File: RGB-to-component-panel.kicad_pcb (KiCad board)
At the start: 2 copper layers, 50 x 70 mm, 60 parts, among them J1 VGA, J3 USB_C_Receptacle_Power, J4 SCART_CONN, J5 3xRCA_CONN, U1 SC6206B-65K5, U101 TPF144-VR, U2 TPF144-VR, U3 RS8752XQ, U6 74AHC1G86, U7 74AHC1G86, U8 LM1881

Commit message: fixed resistor
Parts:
- removed the C1 at (37.8, 77.5)
- removed the C10 at (38.9, 52.7)
- removed the C11 at (57.1, 68.0)
- removed the C12 at (44.9, 90.7)
- removed the C13 at (39.5, 63.3)
- removed the C14 at (45.0, 68.7)
- removed the C2 at (37.8, 81.3)
- removed the C3 at (37.8, 88.9)
- removed the C4 at (40.3, 75.9)
- removed the C5 at (33.7, 44.5)
- removed the C7 at (51.0, 48.0)
- removed the C8 at (39.5, 44.1)
- removed the C9 at (44.6, 49.6)
- removed the D101 at (58.0, 46.9)
- removed the GOTE1 at (54.0, 96.6)
- removed the GOTE2 at (47.8, 80.7)
- removed the J1 at (24.6, 75.0)
- removed the J3 at (18.4, 47.6)
- removed the J4 at (29.4, 98.0)
- removed the J5 at (66.0, 62.0)
- removed the JP1 at (45.5, 57.0)
- removed the JR1 at (69.7, 90.6)
- removed the JU1 at (69.7, 103.6)
- removed the L101 at (30.6, 43.1)
- removed the R1 at (44.6, 47.6)
- removed the R10 at (56.9, 79.0)
- removed the R101 at (54.8, 49.6)
- removed the R11 at (59.0, 69.6)
- removed the R12 at (52.6, 60.0)
- removed the R13 at (50.6, 60.0)
- removed the R14 at (57.1, 64.2)
- removed the R15 at (39.5, 59.4)
- removed the R16 at (29.6, 46.2)
- removed the R17 at (29.6, 48.2)
- removed the R18 at (45.0, 70.7)
- removed the R19 at (33.8, 52.7)
- removed the R2 at (40.8, 47.6)
- removed the R20 at (45.6, 80.7)
- removed the R21 at (45.6, 82.7)
- removed the R22 at (45.6, 84.7)
- removed the R23 at (42.5, 83.6)
- removed the R24 at (57.1, 71.9)
- removed the R25 at (55.1, 71.9)
- removed the R26 at (52.8, 71.9)
- removed the R27 at (48.8, 71.9)
- removed the R28 at (50.8, 71.9)
- removed the R3 at (37.8, 73.7)
- removed the R4 at (37.8, 85.1)
- removed the R5 at (37.8, 92.7)
- removed the R6 at (56.6, 60.0)
- removed the R7 at (54.6, 60.0)
- removed the R8 at (54.9, 79.0)
- removed the R9 at (57.9, 54.0)
- removed the U1 at (42.7, 44.1)
- removed the U101 at (43.6, 76.6)
- removed the U2 at (44.9, 88.0)
- removed the U3 at (54.1, 66.0)
- removed the U6 at (33.8, 55.6)
- removed the U7 at (38.8, 55.6)
- removed the U8 at (45.0, 64.9)
- added C1: 1u, Capacitor_SMD:C_0805_2012Metric_Pad1.15x1.40mm_HandSolder, F.Cu at (37.6, 77.5)
- added C1: 1u, Capacitor_SMD:C_0805_2012Metric_Pad1.15x1.40mm_HandSolder, F.Cu at (90.6, 77.5)
- added C1: 1u, Capacitor_SMD:C_0805_2012Metric_Pad1.15x1.40mm_HandSolder, F.Cu at (37.6, 150.5)
- added C1: 1u, Capacitor_SMD:C_0805_2012Metric_Pad1.15x1.40mm_HandSolder, F.Cu at (90.6, 150.5)
- added C10: 100n, Capacitor_SMD:C_0805_2012Metric_Pad1.15x1.40mm_HandSolder, F.Cu at (38.7, 52.7)
- added C10: 100n, Capacitor_SMD:C_0805_2012Metric_Pad1.15x1.40mm_HandSolder, F.Cu at (91.7, 52.7)
- added C10: 100n, Capacitor_SMD:C_0805_2012Metric_Pad1.15x1.40mm_HandSolder, F.Cu at (38.7, 125.7)
- added C10: 100n, Capacitor_SMD:C_0805_2012Metric_Pad1.15x1.40mm_HandSolder, F.Cu at (91.7, 125.7)
- added C11: 100n, Capacitor_SMD:C_0805_2012Metric_Pad1.15x1.40mm_HandSolder, F.Cu at (56.9, 68.0)
- added C11: 100n, Capacitor_SMD:C_0805_2012Metric_Pad1.15x1.40mm_HandSolder, F.Cu at (109.9, 68.0)
- added C11: 100n, Capacitor_SMD:C_0805_2012Metric_Pad1.15x1.40mm_HandSolder, F.Cu at (56.9, 141.0)
- added C11: 100n, Capacitor_SMD:C_0805_2012Metric_Pad1.15x1.40mm_HandSolder, F.Cu at (109.9, 141.0)
- added C12: 100n, Capacitor_SMD:C_0805_2012Metric_Pad1.15x1.40mm_HandSolder, F.Cu at (44.7, 90.7)
- added C12: 100n, Capacitor_SMD:C_0805_2012Metric_Pad1.15x1.40mm_HandSolder, F.Cu at (97.7, 90.7)
- added C12: 100n, Capacitor_SMD:C_0805_2012Metric_Pad1.15x1.40mm_HandSolder, F.Cu at (44.7, 163.7)
- added C12: 100n, Capacitor_SMD:C_0805_2012Metric_Pad1.15x1.40mm_HandSolder, F.Cu at (97.7, 163.7)
- added C13: 100n, Capacitor_SMD:C_0805_2012Metric_Pad1.15x1.40mm_HandSolder, F.Cu at (39.3, 63.3)
- added C13: 100n, Capacitor_SMD:C_0805_2012Metric_Pad1.15x1.40mm_HandSolder, F.Cu at (92.3, 63.3)
- added C13: 100n, Capacitor_SMD:C_0805_2012Metric_Pad1.15x1.40mm_HandSolder, F.Cu at (39.3, 136.3)
- added C13: 100n, Capacitor_SMD:C_0805_2012Metric_Pad1.15x1.40mm_HandSolder, F.Cu at (92.3, 136.3)
- added C14: 100n, Capacitor_SMD:C_0805_2012Metric_Pad1.15x1.40mm_HandSolder, F.Cu at (44.8, 68.7)
- added C14: 100n, Capacitor_SMD:C_0805_2012Metric_Pad1.15x1.40mm_HandSolder, F.Cu at (97.8, 68.7)
- added C14: 100n, Capacitor_SMD:C_0805_2012Metric_Pad1.15x1.40mm_HandSolder, F.Cu at (44.8, 141.7)
- added C14: 100n, Capacitor_SMD:C_0805_2012Metric_Pad1.15x1.40mm_HandSolder, F.Cu at (97.8, 141.7)
- added C2: 1u, Capacitor_SMD:C_0805_2012Metric_Pad1.15x1.40mm_HandSolder, F.Cu at (37.6, 81.3)
- added C2: 1u, Capacitor_SMD:C_0805_2012Metric_Pad1.15x1.40mm_HandSolder, F.Cu at (90.6, 81.3)
- added C2: 1u, Capacitor_SMD:C_0805_2012Metric_Pad1.15x1.40mm_HandSolder, F.Cu at (37.6, 154.3)
- added C2: 1u, Capacitor_SMD:C_0805_2012Metric_Pad1.15x1.40mm_HandSolder, F.Cu at (90.6, 154.3)
- added C3: 1u, Capacitor_SMD:C_0805_2012Metric_Pad1.15x1.40mm_HandSolder, F.Cu at (37.6, 88.9)
- added C3: 1u, Capacitor_SMD:C_0805_2012Metric_Pad1.15x1.40mm_HandSolder, F.Cu at (90.6, 88.9)
- added C3: 1u, Capacitor_SMD:C_0805_2012Metric_Pad1.15x1.40mm_HandSolder, F.Cu at (37.6, 161.9)
- added C3: 1u, Capacitor_SMD:C_0805_2012Metric_Pad1.15x1.40mm_HandSolder, F.Cu at (90.6, 161.9)
- added C4: 100n, Capacitor_SMD:C_0805_2012Metric_Pad1.15x1.40mm_HandSolder, F.Cu at (40.1, 75.9)
- added C4: 100n, Capacitor_SMD:C_0805_2012Metric_Pad1.15x1.40mm_HandSolder, F.Cu at (93.1, 75.9)
- added C4: 100n, Capacitor_SMD:C_0805_2012Metric_Pad1.15x1.40mm_HandSolder, F.Cu at (40.1, 148.9)
- added C4: 100n, Capacitor_SMD:C_0805_2012Metric_Pad1.15x1.40mm_HandSolder, F.Cu at (93.1, 148.9)
- added C5: 10u, Capacitor_Tantalum_SMD:CP_EIA-3216-18_Kemet-A_Pad1.58x1.35mm_HandSolder, F.Cu at (33.5, 44.5)
- added C5: 10u, Capacitor_Tantalum_SMD:CP_EIA-3216-18_Kemet-A_Pad1.58x1.35mm_HandSolder, F.Cu at (86.5, 44.5)
- added C5: 10u, Capacitor_Tantalum_SMD:CP_EIA-3216-18_Kemet-A_Pad1.58x1.35mm_HandSolder, F.Cu at (33.5, 117.5)
- added C5: 10u, Capacitor_Tantalum_SMD:CP_EIA-3216-18_Kemet-A_Pad1.58x1.35mm_HandSolder, F.Cu at (86.5, 117.5)
- added C7: 100u, Capacitor_Tantalum_SMD:CP_EIA-3528-21_Kemet-B_Pad1.50x2.35mm_HandSolder, F.Cu at (50.8, 48.0)
- added C7: 100u, Capacitor_Tantalum_SMD:CP_EIA-3528-21_Kemet-B_Pad1.50x2.35mm_HandSolder, F.Cu at (103.8, 48.0)
- added C7: 100u, Capacitor_Tantalum_SMD:CP_EIA-3528-21_Kemet-B_Pad1.50x2.35mm_HandSolder, F.Cu at (50.8, 121.0)
- added C7: 100u, Capacitor_Tantalum_SMD:CP_EIA-3528-21_Kemet-B_Pad1.50x2.35mm_HandSolder, F.Cu at (103.8, 121.0)
- added C8: 100n, Capacitor_SMD:C_0805_2012Metric_Pad1.15x1.40mm_HandSolder, F.Cu at (39.3, 44.1)
- added C8: 100n, Capacitor_SMD:C_0805_2012Metric_Pad1.15x1.40mm_HandSolder, F.Cu at (92.3, 44.1)
- added C8: 100n, Capacitor_SMD:C_0805_2012Metric_Pad1.15x1.40mm_HandSolder, F.Cu at (39.3, 117.1)
- added C8: 100n, Capacitor_SMD:C_0805_2012Metric_Pad1.15x1.40mm_HandSolder, F.Cu at (92.3, 117.1)
- added C9: 10u, Capacitor_SMD:C_0805_2012Metric_Pad1.15x1.40mm_HandSolder, F.Cu at (44.4, 49.6)
- added C9: 10u, Capacitor_SMD:C_0805_2012Metric_Pad1.15x1.40mm_HandSolder, F.Cu at (97.4, 49.6)
- added C9: 10u, Capacitor_SMD:C_0805_2012Metric_Pad1.15x1.40mm_HandSolder, F.Cu at (44.4, 122.6)
- added C9: 10u, Capacitor_SMD:C_0805_2012Metric_Pad1.15x1.40mm_HandSolder, F.Cu at (97.4, 122.6)
- added D101: LED, LED_SMD:LED_0805_2012Metric, F.Cu at (57.8, 46.9)
- added D101: LED, LED_SMD:LED_0805_2012Metric, F.Cu at (110.8, 46.9)
- added D101: LED, LED_SMD:LED_0805_2012Metric, F.Cu at (57.8, 119.9)
- added D101: LED, LED_SMD:LED_0805_2012Metric, F.Cu at (110.8, 119.9)
- added GOTE1: Fiducial, videobits:uwuriel, F.Cu at (53.8, 96.6)
- added GOTE1: Fiducial, videobits:uwuriel, F.Cu at (106.8, 96.6)
- added GOTE1: Fiducial, videobits:uwuriel, F.Cu at (53.8, 169.6)
- added GOTE1: Fiducial, videobits:uwuriel, F.Cu at (106.8, 169.6)
- added GOTE2: Fiducial, videobits:borgar, B.Cu at (47.6, 80.7)
- added GOTE2: Fiducial, videobits:borgar, B.Cu at (100.6, 80.7)
- added GOTE2: Fiducial, videobits:borgar, B.Cu at (47.6, 153.7)
- added GOTE2: Fiducial, videobits:borgar, B.Cu at (100.6, 153.7)
- added J1: VGA, custom_components:VGA_CONN, F.Cu at (24.4, 75.0)
- added J1: VGA, custom_components:VGA_CONN, F.Cu at (77.4, 75.0)
- added J1: VGA, custom_components:VGA_CONN, F.Cu at (24.4, 148.0)
- added J1: VGA, custom_components:VGA_CONN, F.Cu at (77.4, 148.0)
- added J3: USB_C_Receptacle_Power, videobits:USB_C_Receptacle_Generic_Power_Only, F.Cu at (18.2, 47.6)
- added J3: USB_C_Receptacle_Power, videobits:USB_C_Receptacle_Generic_Power_Only, F.Cu at (71.2, 47.6)
- added J3: USB_C_Receptacle_Power, videobits:USB_C_Receptacle_Generic_Power_Only, F.Cu at (18.2, 120.6)
- added J3: USB_C_Receptacle_Power, videobits:USB_C_Receptacle_Generic_Power_Only, F.Cu at (71.2, 120.6)
- added J4: SCART_CONN, custom_components:SCART_CONN, F.Cu at (29.2, 98.0)
- added J4: SCART_CONN, custom_components:SCART_CONN, F.Cu at (82.2, 98.0)
- added J4: SCART_CONN, custom_components:SCART_CONN, F.Cu at (29.2, 171.0)
- added J4: SCART_CONN, custom_components:SCART_CONN, F.Cu at (82.2, 171.0)
- added J5: 3xRCA_CONN, custom_components:3xRCA_CONN, F.Cu at (65.8, 62.0)
- added J5: 3xRCA_CONN, custom_components:3xRCA_CONN, F.Cu at (118.8, 62.0)
- added J5: 3xRCA_CONN, custom_components:3xRCA_CONN, F.Cu at (65.8, 135.0)
- added J5: 3xRCA_CONN, custom_components:3xRCA_CONN, F.Cu at (118.8, 135.0)
- added JP1: Jumper_3_Bridged12, Jumper:SolderJumper-3_P1.3mm_Bridged12_Pad1.0x1.5mm, F.Cu at (45.3, 57.0)
- added JP1: Jumper_3_Bridged12, Jumper:SolderJumper-3_P1.3mm_Bridged12_Pad1.0x1.5mm, F.Cu at (98.3, 57.0)
- added JP1: Jumper_3_Bridged12, Jumper:SolderJumper-3_P1.3mm_Bridged12_Pad1.0x1.5mm, F.Cu at (45.3, 130.0)
- added JP1: Jumper_3_Bridged12, Jumper:SolderJumper-3_P1.3mm_Bridged12_Pad1.0x1.5mm, F.Cu at (98.3, 130.0)
- added JR1: Conn_Coaxial, videobits:Cheapo_RCA_single_edge, F.Cu at (69.5, 90.6)
- added JR1: Conn_Coaxial, videobits:Cheapo_RCA_single_edge, F.Cu at (122.5, 90.6)
- added JR1: Conn_Coaxial, videobits:Cheapo_RCA_single_edge, F.Cu at (69.5, 163.6)
- added JR1: Conn_Coaxial, videobits:Cheapo_RCA_single_edge, F.Cu at (122.5, 163.6)
- added JU1: Conn_Coaxial, videobits:Cheapo_RCA_single_edge, F.Cu at (69.5, 103.6)
- added JU1: Conn_Coaxial, videobits:Cheapo_RCA_single_edge, F.Cu at (122.5, 103.6)
- added JU1: Conn_Coaxial, videobits:Cheapo_RCA_single_edge, F.Cu at (69.5, 176.6)
- added JU1: Conn_Coaxial, videobits:Cheapo_RCA_single_edge, F.Cu at (122.5, 176.6)
- added L101: 10u, Inductor_SMD:L_0805_2012Metric_Pad1.15x1.40mm_HandSolder, F.Cu at (30.4, 43.1)
- added L101: 10u, Inductor_SMD:L_0805_2012Metric_Pad1.15x1.40mm_HandSolder, F.Cu at (83.4, 43.1)
- added L101: 10u, Inductor_SMD:L_0805_2012Metric_Pad1.15x1.40mm_HandSolder, F.Cu at (30.4, 116.1)
- added L101: 10u, Inductor_SMD:L_0805_2012Metric_Pad1.15x1.40mm_HandSolder, F.Cu at (83.4, 116.1)
- added R1: 1k, Resistor_SMD:R_0805_2012Metric_Pad1.15x1.40mm_HandSolder, F.Cu at (44.4, 47.6)
- added R1: 1k, Resistor_SMD:R_0805_2012Metric_Pad1.15x1.40mm_HandSolder, F.Cu at (97.4, 47.6)
- added R1: 1k, Resistor_SMD:R_0805_2012Metric_Pad1.15x1.40mm_HandSolder, F.Cu at (44.4, 120.6)
- added R1: 1k, Resistor_SMD:R_0805_2012Metric_Pad1.15x1.40mm_HandSolder, F.Cu at (97.4, 120.6)
- added R10: 75, Resistor_SMD:R_0805_2012Metric_Pad1.15x1.40mm_HandSolder, F.Cu at (56.7, 79.0)
- added R10: 75, Resistor_SMD:R_0805_2012Metric_Pad1.15x1.40mm_HandSolder, F.Cu at (109.7, 79.0)
- added R10: 75, Resistor_SMD:R_0805_2012Metric_Pad1.15x1.40mm_HandSolder, F.Cu at (56.7, 152.0)
- added R10: 75, Resistor_SMD:R_0805_2012Metric_Pad1.15x1.40mm_HandSolder, F.Cu at (109.7, 152.0)
- added R101: 1k, Resistor_SMD:R_0805_2012Metric_Pad1.15x1.40mm_HandSolder, F.Cu at (54.6, 49.6)
- added R101: 1k, Resistor_SMD:R_0805_2012Metric_Pad1.15x1.40mm_HandSolder, F.Cu at (107.6, 49.6)
- added R101: 1k, Resistor_SMD:R_0805_2012Metric_Pad1.15x1.40mm_HandSolder, F.Cu at (54.6, 122.6)
- added R101: 1k, Resistor_SMD:R_0805_2012Metric_Pad1.15x1.40mm_HandSolder, F.Cu at (107.6, 122.6)
- added R11: 75, Resistor_SMD:R_0805_2012Metric_Pad1.15x1.40mm_HandSolder, F.Cu at (58.8, 69.6)
- added R11: 75, Resistor_SMD:R_0805_2012Metric_Pad1.15x1.40mm_HandSolder, F.Cu at (111.8, 69.6)
- added R11: 75, Resistor_SMD:R_0805_2012Metric_Pad1.15x1.40mm_HandSolder, F.Cu at (58.8, 142.6)
- added R11: 75, Resistor_SMD:R_0805_2012Metric_Pad1.15x1.40mm_HandSolder, F.Cu at (111.8, 142.6)
- added R12: 4k7, Resistor_SMD:R_0805_2012Metric_Pad1.15x1.40mm_HandSolder, F.Cu at (52.4, 60.0)
- added R12: 4k7, Resistor_SMD:R_0805_2012Metric_Pad1.15x1.40mm_HandSolder, F.Cu at (105.4, 60.0)
- added R12: 4k7, Resistor_SMD:R_0805_2012Metric_Pad1.15x1.40mm_HandSolder, F.Cu at (52.4, 133.0)
- added R12: 4k7, Resistor_SMD:R_0805_2012Metric_Pad1.15x1.40mm_HandSolder, F.Cu at (105.4, 133.0)
- added R13: 1k27, Resistor_SMD:R_0805_2012Metric_Pad1.15x1.40mm_HandSolder, F.Cu at (50.4, 60.0)
- added R13: 1k27, Resistor_SMD:R_0805_2012Metric_Pad1.15x1.40mm_HandSolder, F.Cu at (103.4, 60.0)
- added R13: 1k27, Resistor_SMD:R_0805_2012Metric_Pad1.15x1.40mm_HandSolder, F.Cu at (50.4, 133.0)
- added R13: 1k27, Resistor_SMD:R_0805_2012Metric_Pad1.15x1.40mm_HandSolder, F.Cu at (103.4, 133.0)
- added R14: 1k, Resistor_SMD:R_0805_2012Metric_Pad1.15x1.40mm_HandSolder, F.Cu at (56.9, 64.2)
- added R14: 1k, Resistor_SMD:R_0805_2012Metric_Pad1.15x1.40mm_HandSolder, F.Cu at (109.9, 64.2)
- added R14: 1k, Resistor_SMD:R_0805_2012Metric_Pad1.15x1.40mm_HandSolder, F.Cu at (56.9, 137.2)
- added R14: 1k, Resistor_SMD:R_0805_2012Metric_Pad1.15x1.40mm_HandSolder, F.Cu at (109.9, 137.2)
- added R15: 75, Resistor_SMD:R_0805_2012Metric_Pad1.15x1.40mm_HandSolder, F.Cu at (39.3, 59.4)
- added R15: 75, Resistor_SMD:R_0805_2012Metric_Pad1.15x1.40mm_HandSolder, F.Cu at (92.3, 59.4)
- added R15: 75, Resistor_SMD:R_0805_2012Metric_Pad1.15x1.40mm_HandSolder, F.Cu at (39.3, 132.4)
- added R15: 75, Resistor_SMD:R_0805_2012Metric_Pad1.15x1.40mm_HandSolder, F.Cu at (92.3, 132.4)
- added R16: 5k1, Resistor_SMD:R_0805_2012Metric_Pad1.15x1.40mm_HandSolder, F.Cu at (29.4, 46.2)
- added R16: 5k1, Resistor_SMD:R_0805_2012Metric_Pad1.15x1.40mm_HandSolder, F.Cu at (82.4, 46.2)
- added R16: 5k1, Resistor_SMD:R_0805_2012Metric_Pad1.15x1.40mm_HandSolder, F.Cu at (29.4, 119.2)
- added R16: 5k1, Resistor_SMD:R_0805_2012Metric_Pad1.15x1.40mm_HandSolder, F.Cu at (82.4, 119.2)
- added R17: 5k1, Resistor_SMD:R_0805_2012Metric_Pad1.15x1.40mm_HandSolder, F.Cu at (29.4, 48.2)
- added R17: 5k1, Resistor_SMD:R_0805_2012Metric_Pad1.15x1.40mm_HandSolder, F.Cu at (82.4, 48.2)
- added R17: 5k1, Resistor_SMD:R_0805_2012Metric_Pad1.15x1.40mm_HandSolder, F.Cu at (29.4, 121.2)
- added R17: 5k1, Resistor_SMD:R_0805_2012Metric_Pad1.15x1.40mm_HandSolder, F.Cu at (82.4, 121.2)
- added R18: 680k, Resistor_SMD:R_0805_2012Metric_Pad1.15x1.40mm_HandSolder, F.Cu at (44.8, 70.7)
- added R18: 680k, Resistor_SMD:R_0805_2012Metric_Pad1.15x1.40mm_HandSolder, F.Cu at (97.8, 70.7)
- added R18: 680k, Resistor_SMD:R_0805_2012Metric_Pad1.15x1.40mm_HandSolder, F.Cu at (44.8, 143.7)
- added R18: 680k, Resistor_SMD:R_0805_2012Metric_Pad1.15x1.40mm_HandSolder, F.Cu at (97.8, 143.7)
- added R19: 1k, Resistor_SMD:R_0805_2012Metric_Pad1.15x1.40mm_HandSolder, F.Cu at (33.6, 52.7)
- added R19: 1k, Resistor_SMD:R_0805_2012Metric_Pad1.15x1.40mm_HandSolder, F.Cu at (86.6, 52.7)
- added R19: 1k, Resistor_SMD:R_0805_2012Metric_Pad1.15x1.40mm_HandSolder, F.Cu at (33.6, 125.7)
- added R19: 1k, Resistor_SMD:R_0805_2012Metric_Pad1.15x1.40mm_HandSolder, F.Cu at (86.6, 125.7)
- added R2: 1k33, Resistor_SMD:R_0805_2012Metric_Pad1.15x1.40mm_HandSolder, F.Cu at (40.6, 47.6)
- added R2: 1k33, Resistor_SMD:R_0805_2012Metric_Pad1.15x1.40mm_HandSolder, F.Cu at (93.6, 47.6)
- added R2: 1k33, Resistor_SMD:R_0805_2012Metric_Pad1.15x1.40mm_HandSolder, F.Cu at (40.6, 120.6)
- added R2: 1k33, Resistor_SMD:R_0805_2012Metric_Pad1.15x1.40mm_HandSolder, F.Cu at (93.6, 120.6)
- added R20: 1k, Resistor_SMD:R_0805_2012Metric_Pad1.15x1.40mm_HandSolder, F.Cu at (45.4, 80.7)
- added R20: 1k, Resistor_SMD:R_0805_2012Metric_Pad1.15x1.40mm_HandSolder, F.Cu at (98.4, 80.7)
- added R20: 1k, Resistor_SMD:R_0805_2012Metric_Pad1.15x1.40mm_HandSolder, F.Cu at (45.4, 153.7)
- added R20: 1k, Resistor_SMD:R_0805_2012Metric_Pad1.15x1.40mm_HandSolder, F.Cu at (98.4, 153.7)
- added R21: 511, Resistor_SMD:R_0805_2012Metric_Pad1.15x1.40mm_HandSolder, F.Cu at (45.4, 82.7)
- added R21: 511, Resistor_SMD:R_0805_2012Metric_Pad1.15x1.40mm_HandSolder, F.Cu at (98.4, 82.7)
- added R21: 511, Resistor_SMD:R_0805_2012Metric_Pad1.15x1.40mm_HandSolder, F.Cu at (45.4, 155.7)
- added R21: 511, Resistor_SMD:R_0805_2012Metric_Pad1.15x1.40mm_HandSolder, F.Cu at (98.4, 155.7)
- added R22: 2740, Resistor_SMD:R_0805_2012Metric_Pad1.15x1.40mm_HandSolder, F.Cu at (45.4, 84.7)
- added R22: 2740, Resistor_SMD:R_0805_2012Metric_Pad1.15x1.40mm_HandSolder, F.Cu at (98.4, 84.7)
- added R22: 2740, Resistor_SMD:R_0805_2012Metric_Pad1.15x1.40mm_HandSolder, F.Cu at (45.4, 157.7)
- added R22: 2740, Resistor_SMD:R_0805_2012Metric_Pad1.15x1.40mm_HandSolder, F.Cu at (98.4, 157.7)
- added R23: 300, Resistor_SMD:R_0805_2012Metric_Pad1.15x1.40mm_HandSolder, F.Cu at (42.3, 83.6)
- added R23: 300, Resistor_SMD:R_0805_2012Metric_Pad1.15x1.40mm_HandSolder, F.Cu at (95.3, 83.6)
- added R23: 300, Resistor_SMD:R_0805_2012Metric_Pad1.15x1.40mm_HandSolder, F.Cu at (42.3, 156.6)
- added R23: 300, Resistor_SMD:R_0805_2012Metric_Pad1.15x1.40mm_HandSolder, F.Cu at (95.3, 156.6)
- added R24: 1k, Resistor_SMD:R_0805_2012Metric_Pad1.15x1.40mm_HandSolder, F.Cu at (56.9, 71.9)
- added R24: 1k, Resistor_SMD:R_0805_2012Metric_Pad1.15x1.40mm_HandSolder, F.Cu at (109.9, 71.9)
- added R24: 1k, Resistor_SMD:R_0805_2012Metric_Pad1.15x1.40mm_HandSolder, F.Cu at (56.9, 144.9)
- added R24: 1k, Resistor_SMD:R_0805_2012Metric_Pad1.15x1.40mm_HandSolder, F.Cu at (109.9, 144.9)
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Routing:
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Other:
- board size 50 x 70 mm -> 103 x 143 mm

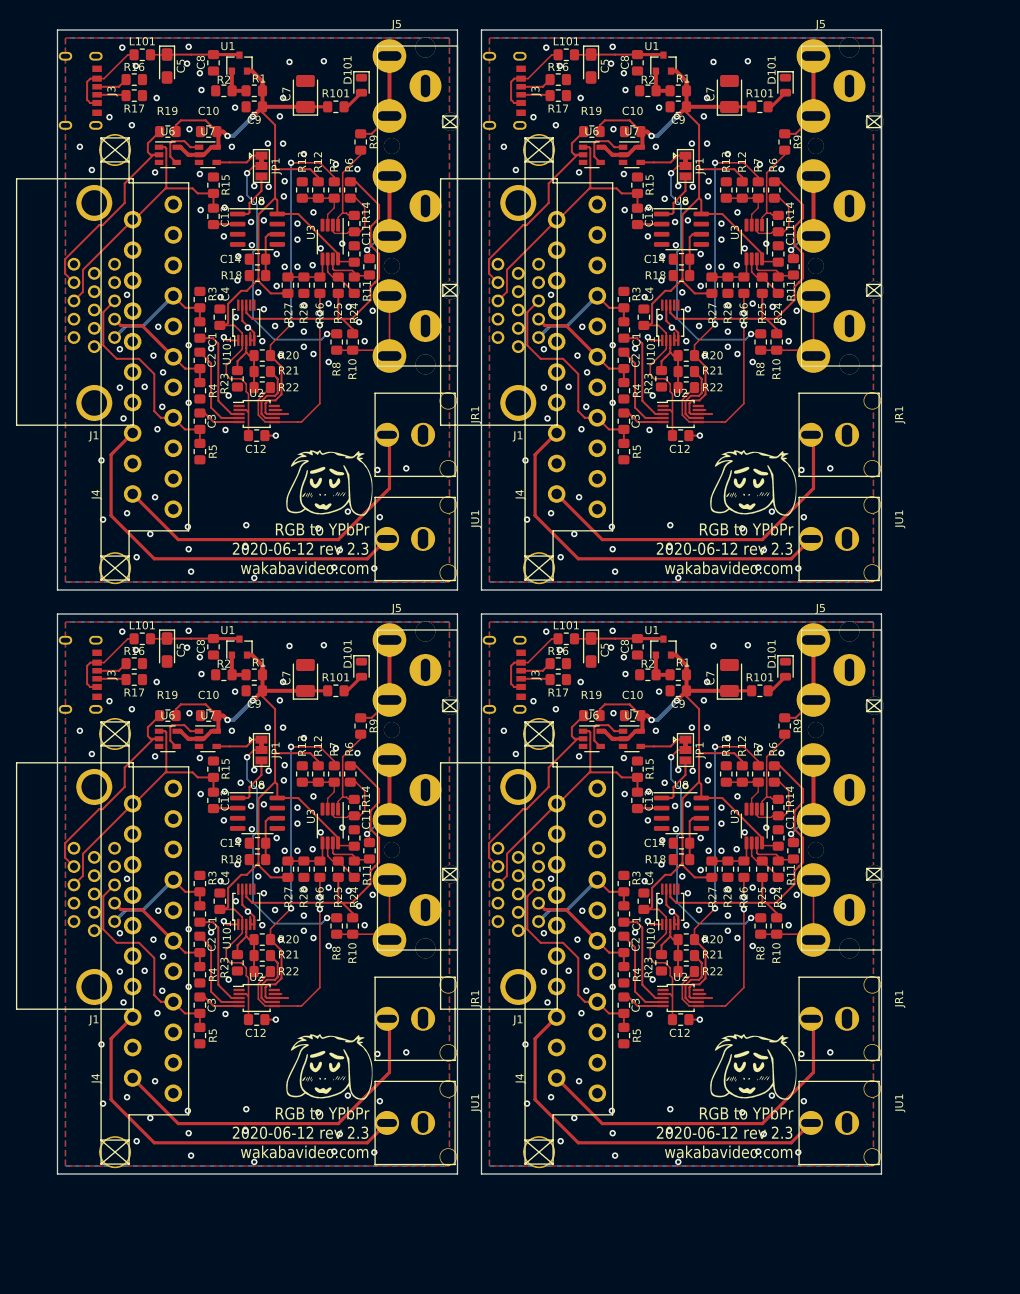
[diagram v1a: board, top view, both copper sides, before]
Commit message: changed RCA jacks to single centre pin style, AHCT gates for VGA sync
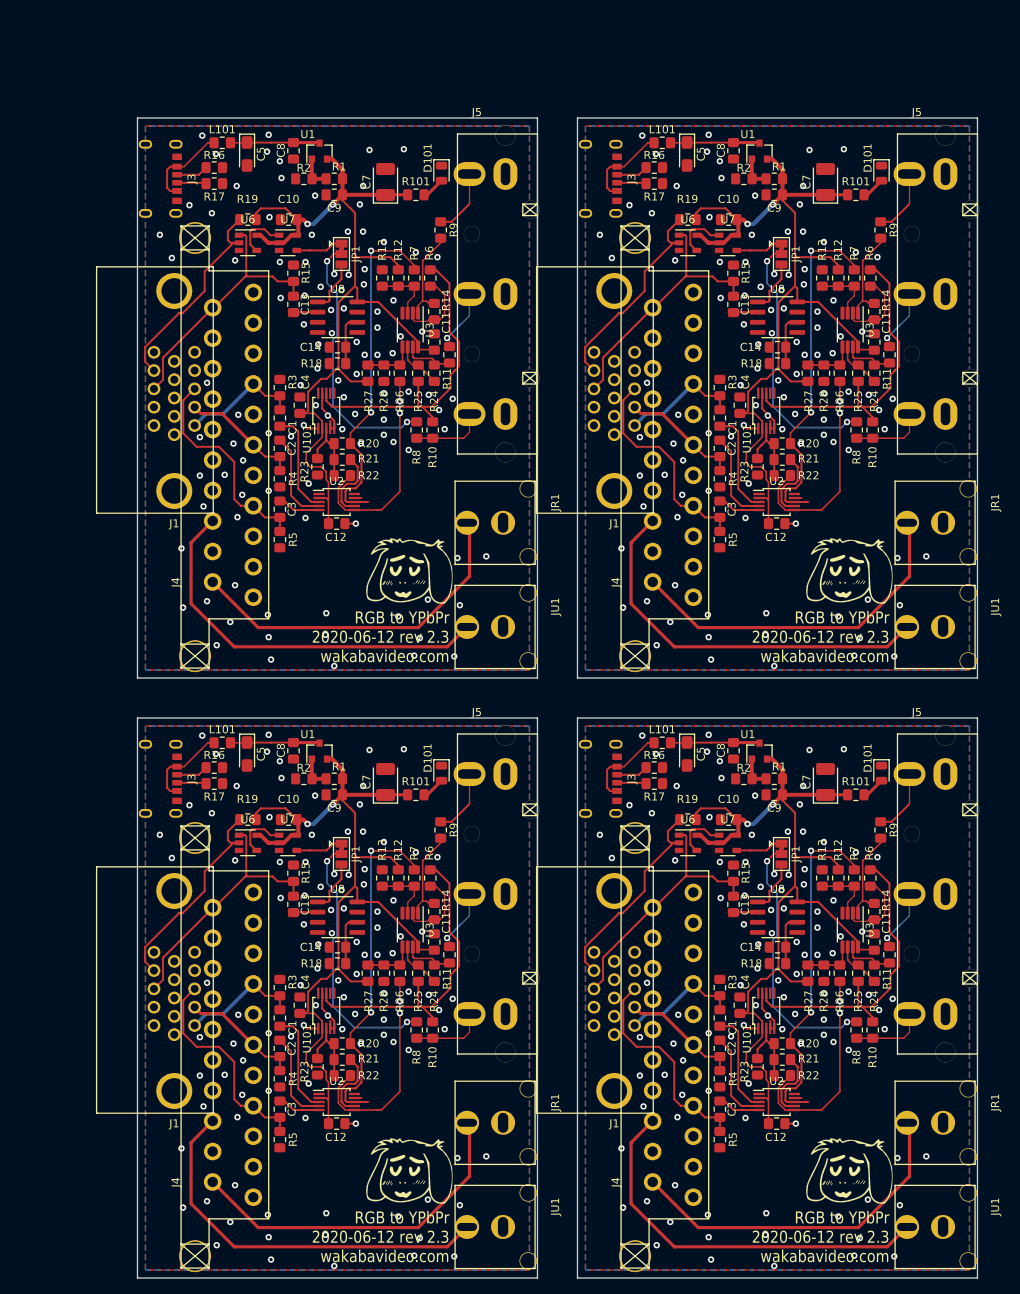
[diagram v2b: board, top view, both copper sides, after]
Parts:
- removed the C1 at (37.6, 77.5)
- removed the C1 at (90.6, 77.5)
- removed the C1 at (37.6, 150.5)
- removed the C1 at (90.6, 150.5)
- removed the C10 at (38.7, 52.7)
- removed the C10 at (91.7, 52.7)
- removed the C10 at (38.7, 125.7)
- removed the C10 at (91.7, 125.7)
- removed the C11 at (56.9, 68.0)
- removed the C11 at (109.9, 68.0)
- removed the C11 at (56.9, 141.0)
- removed the C11 at (109.9, 141.0)
- removed the C12 at (44.7, 90.7)
- removed the C12 at (97.7, 90.7)
- removed the C12 at (44.7, 163.7)
- removed the C12 at (97.7, 163.7)
- removed the C13 at (39.3, 63.3)
- removed the C13 at (92.3, 63.3)
- removed the C13 at (39.3, 136.3)
- removed the C13 at (92.3, 136.3)
- removed the C14 at (44.8, 68.7)
- removed the C14 at (97.8, 68.7)
- removed the C14 at (44.8, 141.7)
- removed the C14 at (97.8, 141.7)
- removed the C2 at (37.6, 81.3)
- removed the C2 at (90.6, 81.3)
- removed the C2 at (37.6, 154.3)
- removed the C2 at (90.6, 154.3)
- removed the C3 at (37.6, 88.9)
- removed the C3 at (90.6, 88.9)
- removed the C3 at (37.6, 161.9)
- removed the C3 at (90.6, 161.9)
- removed the C4 at (40.1, 75.9)
- removed the C4 at (93.1, 75.9)
- removed the C4 at (40.1, 148.9)
- removed the C4 at (93.1, 148.9)
- removed the C5 at (33.5, 44.5)
- removed the C5 at (86.5, 44.5)
- removed the C5 at (33.5, 117.5)
- removed the C5 at (86.5, 117.5)
- removed the C7 at (50.8, 48.0)
- removed the C7 at (103.8, 48.0)
- removed the C7 at (50.8, 121.0)
- removed the C7 at (103.8, 121.0)
- removed the C8 at (39.3, 44.1)
- removed the C8 at (92.3, 44.1)
- removed the C8 at (39.3, 117.1)
- removed the C8 at (92.3, 117.1)
- removed the C9 at (44.4, 49.6)
- removed the C9 at (97.4, 49.6)
- removed the C9 at (44.4, 122.6)
- removed the C9 at (97.4, 122.6)
- removed the D101 at (57.8, 46.9)
- removed the D101 at (110.8, 46.9)
- removed the D101 at (57.8, 119.9)
- removed the D101 at (110.8, 119.9)
- removed the GOTE1 at (53.8, 96.6)
- removed the GOTE1 at (106.8, 96.6)
- removed the GOTE1 at (53.8, 169.6)
- removed the GOTE1 at (106.8, 169.6)
- removed the GOTE2 at (47.6, 80.7)
- removed the GOTE2 at (100.6, 80.7)
- removed the GOTE2 at (47.6, 153.7)
- removed the GOTE2 at (100.6, 153.7)
- removed the J1 at (24.4, 75.0)
- removed the J1 at (77.4, 75.0)
- removed the J1 at (24.4, 148.0)
- removed the J1 at (77.4, 148.0)
- removed the J3 at (18.2, 47.6)
- removed the J3 at (71.2, 47.6)
- removed the J3 at (18.2, 120.6)
- removed the J3 at (71.2, 120.6)
- removed the J4 at (29.2, 98.0)
- removed the J4 at (82.2, 98.0)
- removed the J4 at (29.2, 171.0)
- removed the J4 at (82.2, 171.0)
- removed the J5 at (65.8, 62.0)
- removed the J5 at (118.8, 62.0)
- removed the J5 at (65.8, 135.0)
- removed the J5 at (118.8, 135.0)
- removed the JP1 at (45.3, 57.0)
- removed the JP1 at (98.3, 57.0)
- removed the JP1 at (45.3, 130.0)
- removed the JP1 at (98.3, 130.0)
- removed the JR1 at (69.5, 90.6)
- removed the JR1 at (122.5, 90.6)
- removed the JR1 at (69.5, 163.6)
- removed the JR1 at (122.5, 163.6)
- removed the JU1 at (69.5, 103.6)
- removed the JU1 at (122.5, 103.6)
- removed the JU1 at (69.5, 176.6)
- removed the JU1 at (122.5, 176.6)
- removed the L101 at (30.4, 43.1)
- removed the L101 at (83.4, 43.1)
- removed the L101 at (30.4, 116.1)
- removed the L101 at (83.4, 116.1)
- removed the R1 at (44.4, 47.6)
- removed the R1 at (97.4, 47.6)
- removed the R1 at (44.4, 120.6)
- removed the R1 at (97.4, 120.6)
- removed the R10 at (56.7, 79.0)
- removed the R10 at (109.7, 79.0)
- removed the R10 at (56.7, 152.0)
- removed the R10 at (109.7, 152.0)
- removed the R101 at (54.6, 49.6)
- removed the R101 at (107.6, 49.6)
- removed the R101 at (54.6, 122.6)
- removed the R101 at (107.6, 122.6)
- removed the R11 at (58.8, 69.6)
- removed the R11 at (111.8, 69.6)
- removed the R11 at (58.8, 142.6)
- removed the R11 at (111.8, 142.6)
- removed the R12 at (52.4, 60.0)
- removed the R12 at (105.4, 60.0)
- removed the R12 at (52.4, 133.0)
- removed the R12 at (105.4, 133.0)
- removed the R13 at (50.4, 60.0)
- removed the R13 at (103.4, 60.0)
- removed the R13 at (50.4, 133.0)
- removed the R13 at (103.4, 133.0)
- removed the R14 at (56.9, 64.2)
- removed the R14 at (109.9, 64.2)
- removed the R14 at (56.9, 137.2)
- removed the R14 at (109.9, 137.2)
- removed the R15 at (39.3, 59.4)
- removed the R15 at (92.3, 59.4)
- removed the R15 at (39.3, 132.4)
- removed the R15 at (92.3, 132.4)
- removed the R16 at (29.4, 46.2)
- removed the R16 at (82.4, 46.2)
- removed the R16 at (29.4, 119.2)
- removed the R16 at (82.4, 119.2)
- removed the R17 at (29.4, 48.2)
- removed the R17 at (82.4, 48.2)
- removed the R17 at (29.4, 121.2)
- removed the R17 at (82.4, 121.2)
- removed the R18 at (44.8, 70.7)
- removed the R18 at (97.8, 70.7)
- removed the R18 at (44.8, 143.7)
- removed the R18 at (97.8, 143.7)
- removed the R19 at (33.6, 52.7)
- removed the R19 at (86.6, 52.7)
- removed the R19 at (33.6, 125.7)
- removed the R19 at (86.6, 125.7)
- removed the R2 at (40.6, 47.6)
- removed the R2 at (93.6, 47.6)
- removed the R2 at (40.6, 120.6)
- removed the R2 at (93.6, 120.6)
- removed the R20 at (45.4, 80.7)
- removed the R20 at (98.4, 80.7)
- removed the R20 at (45.4, 153.7)
- removed the R20 at (98.4, 153.7)
- removed the R21 at (45.4, 82.7)
- removed the R21 at (98.4, 82.7)
- removed the R21 at (45.4, 155.7)
- removed the R21 at (98.4, 155.7)
- removed the R22 at (45.4, 84.7)
- removed the R22 at (98.4, 84.7)
- removed the R22 at (45.4, 157.7)
- removed the R22 at (98.4, 157.7)
- removed the R23 at (42.3, 83.6)
- removed the R23 at (95.3, 83.6)
- removed the R23 at (42.3, 156.6)
- removed the R23 at (95.3, 156.6)
- removed the R24 at (56.9, 71.9)
- removed the R24 at (109.9, 71.9)
- removed the R24 at (56.9, 144.9)
- removed the R24 at (109.9, 144.9)
- removed the R25 at (54.9, 71.9)
- removed the R25 at (107.9, 71.9)
- removed the R25 at (54.9, 144.9)
- removed the R25 at (107.9, 144.9)
- removed the R26 at (52.6, 71.9)
- removed the R26 at (105.6, 71.9)
- removed the R26 at (52.6, 144.9)
- removed the R26 at (105.6, 144.9)
- removed the R27 at (48.6, 71.9)
- removed the R27 at (101.6, 71.9)
- removed the R27 at (48.6, 144.9)
- removed the R27 at (101.6, 144.9)
- removed the R28 at (50.6, 71.9)
- removed the R28 at (103.6, 71.9)
- removed the R28 at (50.6, 144.9)
- removed the R28 at (103.6, 144.9)
- removed the R3 at (37.6, 73.7)
- removed the R3 at (90.6, 73.7)
- removed the R3 at (37.6, 146.7)
- removed the R3 at (90.6, 146.7)
- removed the R4 at (37.6, 85.1)
- removed the R4 at (90.6, 85.1)
- removed the R4 at (37.6, 158.1)
- removed the R4 at (90.6, 158.1)
- removed the R5 at (37.6, 92.7)
- removed the R5 at (90.6, 92.7)
- removed the R5 at (37.6, 165.7)
- removed the R5 at (90.6, 165.7)
- removed the R6 at (56.4, 60.0)
- removed the R6 at (109.4, 60.0)
- removed the R6 at (56.4, 133.0)
- removed the R6 at (109.4, 133.0)
- removed the R7 at (54.4, 60.0)
- removed the R7 at (107.4, 60.0)
- removed the R7 at (54.4, 133.0)
- removed the R7 at (107.4, 133.0)
- removed the R8 at (54.7, 79.0)
- removed the R8 at (107.7, 79.0)
- removed the R8 at (54.7, 152.0)
- removed the R8 at (107.7, 152.0)
- removed the R9 at (57.7, 54.0)
- removed the R9 at (110.7, 54.0)
- removed the R9 at (57.7, 127.0)
- removed the R9 at (110.7, 127.0)
- removed the U1 at (42.5, 44.1)
- removed the U1 at (95.5, 44.1)
- removed the U1 at (42.5, 117.1)
- removed the U1 at (95.5, 117.1)
- removed the U101 at (43.4, 76.6)
- removed the U101 at (96.4, 76.6)
- removed the U101 at (43.4, 149.6)
- removed the U101 at (96.4, 149.6)
- removed the U2 at (44.7, 88.0)
- removed the U2 at (97.7, 88.0)
- removed the U2 at (44.7, 161.0)
- removed the U2 at (97.7, 161.0)
- removed the U3 at (53.9, 66.5)
- removed the U3 at (106.9, 66.5)
- removed the U3 at (53.9, 139.5)
- removed the U3 at (106.9, 139.5)
- removed the U6 at (33.6, 55.6)
- removed the U6 at (86.6, 55.6)
- removed the U6 at (33.6, 128.6)
- removed the U6 at (86.6, 128.6)
- removed the U7 at (38.6, 55.6)
- removed the U7 at (91.6, 55.6)
- removed the U7 at (38.6, 128.6)
- removed the U7 at (91.6, 128.6)
- removed the U8 at (44.8, 64.9)
- removed the U8 at (97.8, 64.9)
- removed the U8 at (44.8, 137.9)
- removed the U8 at (97.8, 137.9)
- added C1: 1u, Capacitor_SMD:C_0805_2012Metric_Pad1.15x1.40mm_HandSolder, F.Cu at (102.6, 163.5)
- added C1: 1u, Capacitor_SMD:C_0805_2012Metric_Pad1.15x1.40mm_HandSolder, F.Cu at (47.6, 163.5)
- added C1: 1u, Capacitor_SMD:C_0805_2012Metric_Pad1.15x1.40mm_HandSolder, F.Cu at (47.6, 88.5)
- added C1: 1u, Capacitor_SMD:C_0805_2012Metric_Pad1.15x1.40mm_HandSolder, F.Cu at (102.6, 88.5)
- added C10: 100n, Capacitor_SMD:C_0805_2012Metric_Pad1.15x1.40mm_HandSolder, F.Cu at (103.7, 138.7)
- added C10: 100n, Capacitor_SMD:C_0805_2012Metric_Pad1.15x1.40mm_HandSolder, F.Cu at (48.7, 138.7)
- added C10: 100n, Capacitor_SMD:C_0805_2012Metric_Pad1.15x1.40mm_HandSolder, F.Cu at (48.7, 63.7)
- added C10: 100n, Capacitor_SMD:C_0805_2012Metric_Pad1.15x1.40mm_HandSolder, F.Cu at (103.7, 63.7)
- added C11: 100n, Capacitor_SMD:C_0805_2012Metric_Pad1.15x1.40mm_HandSolder, F.Cu at (121.9, 154.0)
- added C11: 100n, Capacitor_SMD:C_0805_2012Metric_Pad1.15x1.40mm_HandSolder, F.Cu at (66.9, 154.0)
- added C11: 100n, Capacitor_SMD:C_0805_2012Metric_Pad1.15x1.40mm_HandSolder, F.Cu at (66.9, 79.0)
- added C11: 100n, Capacitor_SMD:C_0805_2012Metric_Pad1.15x1.40mm_HandSolder, F.Cu at (121.9, 79.0)
- added C12: 100n, Capacitor_SMD:C_0805_2012Metric_Pad1.15x1.40mm_HandSolder, F.Cu at (109.7, 176.7)
- added C12: 100n, Capacitor_SMD:C_0805_2012Metric_Pad1.15x1.40mm_HandSolder, F.Cu at (54.7, 176.7)
- added C12: 100n, Capacitor_SMD:C_0805_2012Metric_Pad1.15x1.40mm_HandSolder, F.Cu at (54.7, 101.7)
- added C12: 100n, Capacitor_SMD:C_0805_2012Metric_Pad1.15x1.40mm_HandSolder, F.Cu at (109.7, 101.7)
- added C13: 100n, Capacitor_SMD:C_0805_2012Metric_Pad1.15x1.40mm_HandSolder, F.Cu at (104.3, 149.3)
- added C13: 100n, Capacitor_SMD:C_0805_2012Metric_Pad1.15x1.40mm_HandSolder, F.Cu at (49.3, 149.3)
- added C13: 100n, Capacitor_SMD:C_0805_2012Metric_Pad1.15x1.40mm_HandSolder, F.Cu at (49.3, 74.3)
- added C13: 100n, Capacitor_SMD:C_0805_2012Metric_Pad1.15x1.40mm_HandSolder, F.Cu at (104.3, 74.3)
- added C14: 100n, Capacitor_SMD:C_0805_2012Metric_Pad1.15x1.40mm_HandSolder, F.Cu at (109.8, 154.7)
- added C14: 100n, Capacitor_SMD:C_0805_2012Metric_Pad1.15x1.40mm_HandSolder, F.Cu at (54.8, 154.7)
- added C14: 100n, Capacitor_SMD:C_0805_2012Metric_Pad1.15x1.40mm_HandSolder, F.Cu at (54.8, 79.7)
- added C14: 100n, Capacitor_SMD:C_0805_2012Metric_Pad1.15x1.40mm_HandSolder, F.Cu at (109.8, 79.7)
- added C2: 1u, Capacitor_SMD:C_0805_2012Metric_Pad1.15x1.40mm_HandSolder, F.Cu at (102.6, 167.3)
- added C2: 1u, Capacitor_SMD:C_0805_2012Metric_Pad1.15x1.40mm_HandSolder, F.Cu at (47.6, 167.3)
- added C2: 1u, Capacitor_SMD:C_0805_2012Metric_Pad1.15x1.40mm_HandSolder, F.Cu at (47.6, 92.3)
- added C2: 1u, Capacitor_SMD:C_0805_2012Metric_Pad1.15x1.40mm_HandSolder, F.Cu at (102.6, 92.3)
- added C3: 1u, Capacitor_SMD:C_0805_2012Metric_Pad1.15x1.40mm_HandSolder, F.Cu at (102.6, 174.9)
- added C3: 1u, Capacitor_SMD:C_0805_2012Metric_Pad1.15x1.40mm_HandSolder, F.Cu at (47.6, 174.9)
- added C3: 1u, Capacitor_SMD:C_0805_2012Metric_Pad1.15x1.40mm_HandSolder, F.Cu at (47.6, 99.9)
- added C3: 1u, Capacitor_SMD:C_0805_2012Metric_Pad1.15x1.40mm_HandSolder, F.Cu at (102.6, 99.9)
- added C4: 100n, Capacitor_SMD:C_0805_2012Metric_Pad1.15x1.40mm_HandSolder, F.Cu at (105.1, 161.9)
- added C4: 100n, Capacitor_SMD:C_0805_2012Metric_Pad1.15x1.40mm_HandSolder, F.Cu at (50.1, 161.9)
- added C4: 100n, Capacitor_SMD:C_0805_2012Metric_Pad1.15x1.40mm_HandSolder, F.Cu at (50.1, 86.9)
- added C4: 100n, Capacitor_SMD:C_0805_2012Metric_Pad1.15x1.40mm_HandSolder, F.Cu at (105.1, 86.9)
- added C5: 10u, Capacitor_Tantalum_SMD:CP_EIA-3216-18_Kemet-A_Pad1.58x1.35mm_HandSolder, F.Cu at (98.5, 130.5)
- added C5: 10u, Capacitor_Tantalum_SMD:CP_EIA-3216-18_Kemet-A_Pad1.58x1.35mm_HandSolder, F.Cu at (43.5, 130.5)
- added C5: 10u, Capacitor_Tantalum_SMD:CP_EIA-3216-18_Kemet-A_Pad1.58x1.35mm_HandSolder, F.Cu at (43.5, 55.5)
- added C5: 10u, Capacitor_Tantalum_SMD:CP_EIA-3216-18_Kemet-A_Pad1.58x1.35mm_HandSolder, F.Cu at (98.5, 55.5)
- added C7: 100u, Capacitor_Tantalum_SMD:CP_EIA-3528-21_Kemet-B_Pad1.50x2.35mm_HandSolder, F.Cu at (115.8, 134.0)
- added C7: 100u, Capacitor_Tantalum_SMD:CP_EIA-3528-21_Kemet-B_Pad1.50x2.35mm_HandSolder, F.Cu at (60.8, 134.0)
- added C7: 100u, Capacitor_Tantalum_SMD:CP_EIA-3528-21_Kemet-B_Pad1.50x2.35mm_HandSolder, F.Cu at (60.8, 59.0)
- added C7: 100u, Capacitor_Tantalum_SMD:CP_EIA-3528-21_Kemet-B_Pad1.50x2.35mm_HandSolder, F.Cu at (115.8, 59.0)
- added C8: 100n, Capacitor_SMD:C_0805_2012Metric_Pad1.15x1.40mm_HandSolder, F.Cu at (104.3, 130.1)
- added C8: 100n, Capacitor_SMD:C_0805_2012Metric_Pad1.15x1.40mm_HandSolder, F.Cu at (49.3, 130.1)
- added C8: 100n, Capacitor_SMD:C_0805_2012Metric_Pad1.15x1.40mm_HandSolder, F.Cu at (49.3, 55.1)
- added C8: 100n, Capacitor_SMD:C_0805_2012Metric_Pad1.15x1.40mm_HandSolder, F.Cu at (104.3, 55.1)
- added C9: 10u, Capacitor_SMD:C_0805_2012Metric_Pad1.15x1.40mm_HandSolder, F.Cu at (109.4, 135.6)
- added C9: 10u, Capacitor_SMD:C_0805_2012Metric_Pad1.15x1.40mm_HandSolder, F.Cu at (54.4, 135.6)
- added C9: 10u, Capacitor_SMD:C_0805_2012Metric_Pad1.15x1.40mm_HandSolder, F.Cu at (54.4, 60.6)
- added C9: 10u, Capacitor_SMD:C_0805_2012Metric_Pad1.15x1.40mm_HandSolder, F.Cu at (109.4, 60.6)
- added D101: LED, LED_SMD:LED_0805_2012Metric, F.Cu at (122.8, 132.9)
- added D101: LED, LED_SMD:LED_0805_2012Metric, F.Cu at (67.8, 132.9)
- added D101: LED, LED_SMD:LED_0805_2012Metric, F.Cu at (67.8, 57.9)
- added D101: LED, LED_SMD:LED_0805_2012Metric, F.Cu at (122.8, 57.9)
- added GOTE1: Fiducial, videobits:uwuriel, F.Cu at (118.8, 182.6)
- added GOTE1: Fiducial, videobits:uwuriel, F.Cu at (63.8, 182.6)
- added GOTE1: Fiducial, videobits:uwuriel, F.Cu at (63.8, 107.6)
- added GOTE1: Fiducial, videobits:uwuriel, F.Cu at (118.8, 107.6)
- added GOTE2: Fiducial, videobits:borgar, B.Cu at (112.6, 166.7)
- added GOTE2: Fiducial, videobits:borgar, B.Cu at (57.6, 166.7)
- added GOTE2: Fiducial, videobits:borgar, B.Cu at (57.6, 91.7)
- added GOTE2: Fiducial, videobits:borgar, B.Cu at (112.6, 91.7)
- added J1: VGA, custom_components:VGA_CONN, F.Cu at (89.4, 161.0)
- added J1: VGA, custom_components:VGA_CONN, F.Cu at (34.4, 161.0)
- added J1: VGA, custom_components:VGA_CONN, F.Cu at (34.4, 86.0)
- added J1: VGA, custom_components:VGA_CONN, F.Cu at (89.4, 86.0)
- added J3: USB_C_Receptacle_Power, videobits:USB_C_Receptacle_Generic_Power_Only, F.Cu at (83.2, 133.6)
- added J3: USB_C_Receptacle_Power, videobits:USB_C_Receptacle_Generic_Power_Only, F.Cu at (28.2, 133.6)
- added J3: USB_C_Receptacle_Power, videobits:USB_C_Receptacle_Generic_Power_Only, F.Cu at (28.2, 58.6)
- added J3: USB_C_Receptacle_Power, videobits:USB_C_Receptacle_Generic_Power_Only, F.Cu at (83.2, 58.6)
- added J4: SCART_CONN, custom_components:SCART_CONN, F.Cu at (94.2, 184.0)
- added J4: SCART_CONN, custom_components:SCART_CONN, F.Cu at (39.2, 184.0)
- added J4: SCART_CONN, custom_components:SCART_CONN, F.Cu at (39.2, 109.0)
- added J4: SCART_CONN, custom_components:SCART_CONN, F.Cu at (94.2, 109.0)
- added J5: 3xRCA_CONN, videobits:3xRCA_CONN_SINGLE, F.Cu at (130.8, 148.0)
- added J5: 3xRCA_CONN, videobits:3xRCA_CONN_SINGLE, F.Cu at (75.8, 148.0)
- added J5: 3xRCA_CONN, videobits:3xRCA_CONN_SINGLE, F.Cu at (75.8, 73.0)
- added J5: 3xRCA_CONN, videobits:3xRCA_CONN_SINGLE, F.Cu at (130.8, 73.0)
- added JP1: Jumper_3_Bridged12, Jumper:SolderJumper-3_P1.3mm_Bridged12_Pad1.0x1.5mm, F.Cu at (110.3, 143.0)
- added JP1: Jumper_3_Bridged12, Jumper:SolderJumper-3_P1.3mm_Bridged12_Pad1.0x1.5mm, F.Cu at (55.3, 143.0)
- added JP1: Jumper_3_Bridged12, Jumper:SolderJumper-3_P1.3mm_Bridged12_Pad1.0x1.5mm, F.Cu at (55.3, 68.0)
- added JP1: Jumper_3_Bridged12, Jumper:SolderJumper-3_P1.3mm_Bridged12_Pad1.0x1.5mm, F.Cu at (110.3, 68.0)
- added JR1: Conn_Coaxial, videobits:Cheapo_RCA_single_edge, F.Cu at (134.5, 176.6)
- added JR1: Conn_Coaxial, videobits:Cheapo_RCA_single_edge, F.Cu at (79.5, 176.6)
- added JR1: Conn_Coaxial, videobits:Cheapo_RCA_single_edge, F.Cu at (79.5, 101.6)
- added JR1: Conn_Coaxial, videobits:Cheapo_RCA_single_edge, F.Cu at (134.5, 101.6)
- added JU1: Conn_Coaxial, videobits:Cheapo_RCA_single_edge, F.Cu at (134.5, 189.6)
- added JU1: Conn_Coaxial, videobits:Cheapo_RCA_single_edge, F.Cu at (79.5, 189.6)
- added JU1: Conn_Coaxial, videobits:Cheapo_RCA_single_edge, F.Cu at (79.5, 114.6)
- added JU1: Conn_Coaxial, videobits:Cheapo_RCA_single_edge, F.Cu at (134.5, 114.6)
- added L101: 10u, Inductor_SMD:L_0805_2012Metric_Pad1.15x1.40mm_HandSolder, F.Cu at (95.4, 129.1)
- added L101: 10u, Inductor_SMD:L_0805_2012Metric_Pad1.15x1.40mm_HandSolder, F.Cu at (40.4, 129.1)
- added L101: 10u, Inductor_SMD:L_0805_2012Metric_Pad1.15x1.40mm_HandSolder, F.Cu at (40.4, 54.1)
- added L101: 10u, Inductor_SMD:L_0805_2012Metric_Pad1.15x1.40mm_HandSolder, F.Cu at (95.4, 54.1)
- added R1: 1k, Resistor_SMD:R_0805_2012Metric_Pad1.15x1.40mm_HandSolder, F.Cu at (109.4, 133.6)
- added R1: 1k, Resistor_SMD:R_0805_2012Metric_Pad1.15x1.40mm_HandSolder, F.Cu at (54.4, 133.6)
- added R1: 1k, Resistor_SMD:R_0805_2012Metric_Pad1.15x1.40mm_HandSolder, F.Cu at (54.4, 58.6)
- added R1: 1k, Resistor_SMD:R_0805_2012Metric_Pad1.15x1.40mm_HandSolder, F.Cu at (109.4, 58.6)
- added R10: 75, Resistor_SMD:R_0805_2012Metric_Pad1.15x1.40mm_HandSolder, F.Cu at (121.7, 165.0)
- added R10: 75, Resistor_SMD:R_0805_2012Metric_Pad1.15x1.40mm_HandSolder, F.Cu at (66.7, 165.0)
- added R10: 75, Resistor_SMD:R_0805_2012Metric_Pad1.15x1.40mm_HandSolder, F.Cu at (66.7, 90.0)
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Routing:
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- added copper zone on B.Cu, net (none)
- added copper zone on F.Cu, net (none)
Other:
- board size 103 x 143 mm -> 105 x 145 mm
